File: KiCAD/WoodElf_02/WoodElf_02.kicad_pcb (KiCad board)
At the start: 2 copper layers, 19.2 x 19.2 mm, 14 parts

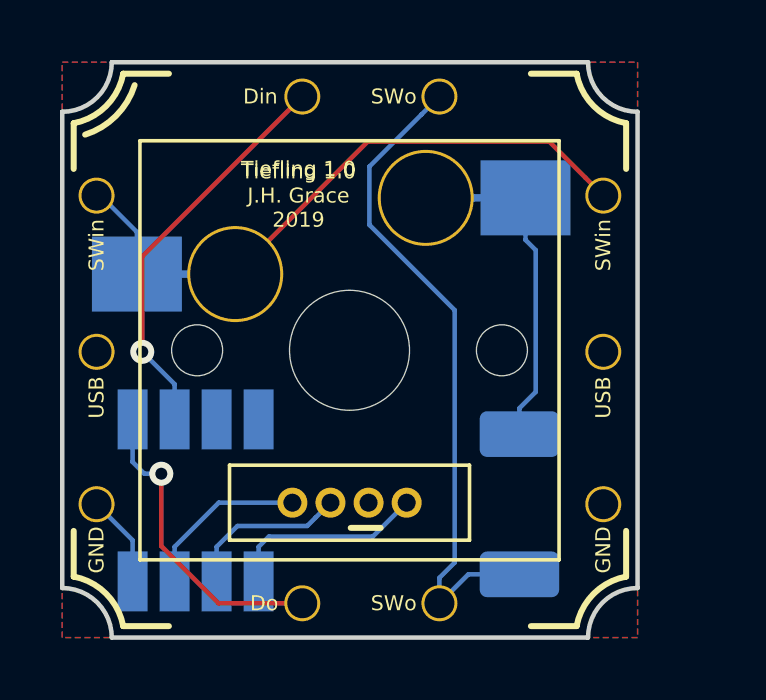
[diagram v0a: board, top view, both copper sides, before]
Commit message: updated the Tiefling PCB to better match real-world screw options
Also started mocking up the 3D-printed section
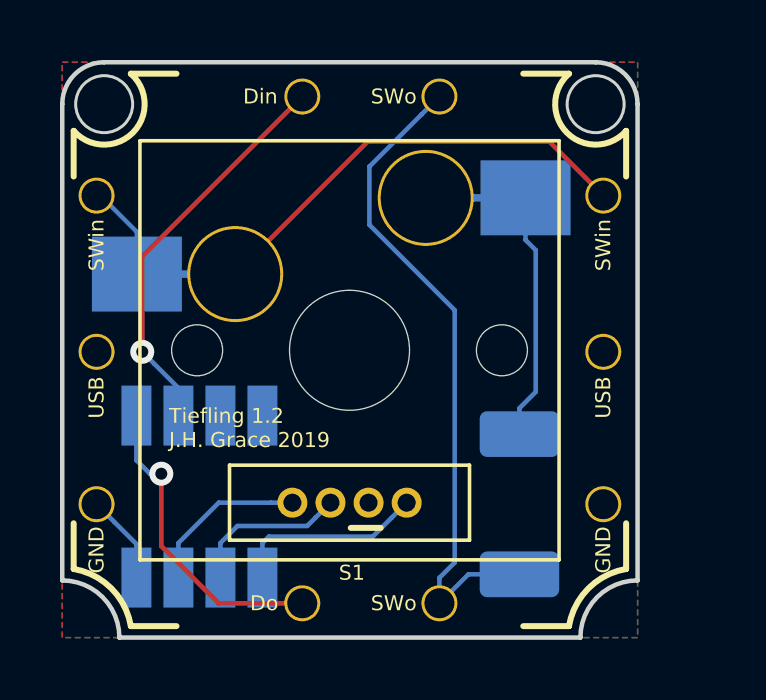
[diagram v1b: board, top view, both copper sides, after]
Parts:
- S1: renamed from Tiefling 1.0
- moved C 0.18 mm to (135.6, 112.5)
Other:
- outline, holes or cut-outs redrawn
- board text added: "Tiefling 1.2 J.H. Grace 2019"
- board text removed: "Tiefling 1.0 J.H. Grace 2019"

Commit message: completely redid the core code
it now uses a key matrix like any other sane keyboard does.  none of this slow-af I2C interface nonsense
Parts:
- added Mount: Mount, WoodElfLib:Mount, F.Cu at (132.5, 99.4)
- added Mount: Mount, WoodElfLib:Mount, F.Cu at (148.8, 99.4)
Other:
- outline, holes or cut-outs redrawn
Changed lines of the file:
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@@
   (general
     (thickness 1.6)
-    (drawings 36)
+    (drawings 34)
     (tracks 57)
     (zones 0)
-    (modules 14)
+    (modules 16)
     (nets 12)
   )
@@
     (add_net "Net-(D1-Pad1)")
   )
+  (module WoodElfLib:Mount (layer F.Cu)
+    (at 132.461 99.441)
+    (fp_text reference Mount (at 0 -1.397) (layer F.Fab)
+      (effects (font (size 0.5 0.5) (thickness 0.125)))
+    )
+    (fp_text value Mount (at 0 -1.397) (layer F.Fab)
+      (effects (font (size 0.5 0.5) (thickness 0.125)))
+    )
+    (pad "" np_thru_hole circle (at 0 0) (size 2 2) (drill 2) (layers *.Cu *.Mask))
+  )
+  (module WoodElfLib:Mount (layer F.Cu)
+    (at 148.844 99.441)
+    (fp_text reference Mount (at 0 -1.397) (layer F.Fab)
+      (effects (font (size 0.5 0.5) (thickness 0.125)))
+    )
+    (fp_text value Mount (at 0 -1.397) (layer F.Fab)
+      (effects (font (size 0.5 0.5) (thickness 0.125)))
+    )
+    (pad "" np_thru_hole circle (at 0 0) (size 2 2) (drill 2) (layers *.Cu *.Mask))
+  )
   (module WoodElfLib:SW_Cherry_MX1A_1.00u_PCB (layer F.Cu)
     (at 143.1798 102.5652)
@@
       (effects (font (size 1 1) (thickness 0.15)))
     )
+    (fp_line (start -10.414 12.954) (end -10.414 -2.794) (layer Dwgs.User) (width 0.15))
+    (fp_line (start 5.334 12.954) (end -10.414 12.954) (layer Dwgs.User) (width 0.15))
+    (fp_line (start 5.334 -2.794) (end 5.334 12.954) (layer Dwgs.User) (width 0.15))
+    (fp_line (start -10.393 -2.794) (end 5.334 -2.794) (layer Dwgs.User) (width 0.15))
+    (fp_line (start -9.525 12.065) (end -9.525 -1.905) (layer F.SilkS) (width 0.12))
+    (fp_line (start 4.445 12.065) (end -9.525 12.065) (layer F.SilkS) (width 0.12))
+    (fp_line (start 4.445 -1.905) (end 4.445 12.065) (layer F.SilkS) (width 0.12))
+    (fp_line (start -9.525 -1.905) (end 4.445 -1.905) (layer F.SilkS) (width 0.12))
+    (fp_line (start -12.065 14.605) (end -12.065 -4.445) (layer Dwgs.User) (width 0.15))
+    (fp_line (start 6.985 14.605) (end -12.065 14.605) (layer Dwgs.User) (width 0.15))
+    (fp_line (start 6.985 -4.445) (end 6.985 14.605) (layer Dwgs.User) (width 0.15))
+    (fp_line (start -12.065 -4.445) (end 6.985 -4.445) (layer Dwgs.User) (width 0.15))
+    (fp_line (start -9.14 -1.52) (end 4.06 -1.52) (layer F.CrtYd) (width 0.05))
+    (fp_line (start 4.06 -1.52) (end 4.06 11.68) (layer F.CrtYd) (width 0.05))
+    (fp_line (start 4.06 11.68) (end -9.14 11.68) (layer F.CrtYd) (width 0.05))
+    (fp_line (start -9.14 11.68) (end -9.14 -1.52) (layer F.CrtYd) (width 0.05))
+    (fp_text user %R (at -2.54 0) (layer F.Fab)
+      (effects (font (size 0.5 0.5) (thickness 0.125)))
+    )
+    (fp_line (start -6.54 8.91) (end -6.54 11.41) (layer F.SilkS) (width 0.12))
+    (fp_line (start -6.54 8.91) (end 1.46 8.91) (layer F.SilkS) (width 0.12))
+    (fp_line (start 1.46 8.91) (end 1.46 11.41) (layer F.SilkS) (width 0.12))
+    (fp_line (start -6.54 11.41) (end 1.46 11.41) (layer F.SilkS) (width 0.12))
     (fp_line (start -2.5 11) (end -1.5 11) (layer F.SilkS) (width 0.2))
-    (fp_line (start -6.54 11.41) (end 1.46 11.41) (layer F.SilkS) (width 0.12))
-    (fp_line (start 1.46 8.91) (end 1.46 11.41) (layer F.SilkS) (width 0.12))
-    (fp_line (start -6.54 8.91) (end 1.46 8.91) (layer F.SilkS) (width 0.12))
-    (fp_line (start -6.54 8.91) (end -6.54 11.41) (layer F.SilkS) (width 0.12))
-    (fp_text user %R (at -2.54 0) (layer F.Fab)
-      (effects (font (size 0.5 0.5) (thickness 0.125)))
-    )
-    (fp_line (start -9.14 11.68) (end -9.14 -1.52) (layer F.CrtYd) (width 0.05))
-    (fp_line (start 4.06 11.68) (end -9.14 11.68) (layer F.CrtYd) (width 0.05))
-    (fp_line (start 4.06 -1.52) (end 4.06 11.68) (layer F.CrtYd) (width 0.05))
-    (fp_line (start -9.14 -1.52) (end 4.06 -1.52) (layer F.CrtYd) (width 0.05))
-    (fp_line (start -12.065 -4.445) (end 6.985 -4.445) (layer Dwgs.User) (width 0.15))
-    (fp_line (start 6.985 -4.445) (end 6.985 14.605) (layer Dwgs.User) (width 0.15))
-    (fp_line (start 6.985 14.605) (end -12.065 14.605) (layer Dwgs.User) (width 0.15))
-    (fp_line (start -12.065 14.605) (end -12.065 -4.445) (layer Dwgs.User) (width 0.15))
-    (fp_line (start -9.525 -1.905) (end 4.445 -1.905) (layer F.SilkS) (width 0.12))
-    (fp_line (start 4.445 -1.905) (end 4.445 12.065) (layer F.SilkS) (width 0.12))
-    (fp_line (start 4.445 12.065) (end -9.525 12.065) (layer F.SilkS) (width 0.12))
-    (fp_line (start -9.525 12.065) (end -9.525 -1.905) (layer F.SilkS) (width 0.12))
+    (pad "" np_thru_hole circle (at 2.54 5.08) (size 1.7 1.7) (drill 1.7) (layers *.Cu *.Mask))
+    (pad "" np_thru_hole circle (at -7.62 5.08) (size 1.7 1.7) (drill 1.7) (layers *.Cu *.Mask))
+    (pad "" np_thru_hole circle (at -2.54 5.08) (size 4 4) (drill 4) (layers *.Cu *.Mask))
+    (pad 2 thru_hole circle (at -6.35 2.54) (size 3.2 3.2) (drill 3) (layers *.Cu *.Mask)
+      (net 11 /SWIN))
+    (pad 1 thru_hole circle (at 0 0) (size 3.2 3.2) (drill 3) (layers *.Cu *.Mask)
+      (net 6 "Net-(D1-Pad1)"))
+    (pad 5 thru_hole circle (at -3.175 10.16) (size 1 1) (drill 0.6) (layers *.Cu *.Mask)
+      (net 1 "Net-(C1-Pad2)") (solder_mask_margin 0.1) (clearance 0.01))
+    (pad 6 thru_hole circle (at -4.445 10.16) (size 1 1) (drill 0.6) (layers *.Cu *.Mask)
+      (net 2 "Net-(C1-Pad3)") (solder_mask_margin 0.1) (clearance 0.01))
+    (pad 4 thru_hole circle (at -1.905 10.16 45) (size 1 1) (drill 0.6) (layers *.Cu *.Mask)
+      (net 5 /USB) (solder_mask_margin 0.1) (clearance 0.01))
     (pad 3 thru_hole circle (at -0.635 10.16) (size 1 1) (drill 0.6) (layers *.Cu *.Mask)
       (net 3 "Net-(C1-Pad1)") (solder_mask_margin 0.1) (clearance 0.01))
-    (pad 4 thru_hole circle (at -1.905 10.16 45) (size 1 1) (drill 0.6) (layers *.Cu *.Mask)
-      (net 5 /USB) (solder_mask_margin 0.1) (clearance 0.01))
-    (pad 6 thru_hole circle (at -4.445 10.16) (size 1 1) (drill 0.6) (layers *.Cu *.Mask)
-      (net 2 "Net-(C1-Pad3)") (solder_mask_margin 0.1) (clearance 0.01))
-    (pad 5 thru_hole circle (at -3.175 10.16) (size 1 1) (drill 0.6) (layers *.Cu *.Mask)
-      (net 1 "Net-(C1-Pad2)") (solder_mask_margin 0.1) (clearance 0.01))
-    (pad 1 thru_hole circle (at 0 0) (size 3.2 3.2) (drill 3) (layers *.Cu *.Mask)
-      (net 6 "Net-(D1-Pad1)"))
-    (pad 2 thru_hole circle (at -6.35 2.54) (size 3.2 3.2) (drill 3) (layers *.Cu *.Mask)
-      (net 11 /SWIN))
-    (pad "" np_thru_hole circle (at -2.54 5.08) (size 4 4) (drill 4) (layers *.Cu *.Mask))
-    (pad "" np_thru_hole circle (at -7.62 5.08) (size 1.7 1.7) (drill 1.7) (layers *.Cu *.Mask))
-    (pad "" np_thru_hole circle (at 2.54 5.08) (size 1.7 1.7) (drill 1.7) (layers *.Cu *.Mask))
     (model ${KISYS3DMOD}/Button_Switch_Keyboard.3dshapes/SW_Cherry_MX1A_1.00u_PCB.wrl
       (at (xyz 0 0 0))
@@
   )
   (gr_arc (start 148.844 99.441) (end 147.955 98.425) (angle -187.6281497) (layer B.SilkS) (width 0.2))
-  (gr_circle (center 132.461 99.441) (end 133.411 99.441) (layer Edge.Cuts) (width 0.1))
-  (gr_circle (center 148.844 99.441) (end 149.794 99.441) (layer Edge.Cuts) (width 0.1))
   (gr_line (start 147.955 98.425) (end 146.431 98.425) (layer B.SilkS) (width 0.2))
   (gr_line (start 149.86 100.33) (end 149.86 101.854) (layer B.SilkS) (width 0.2))

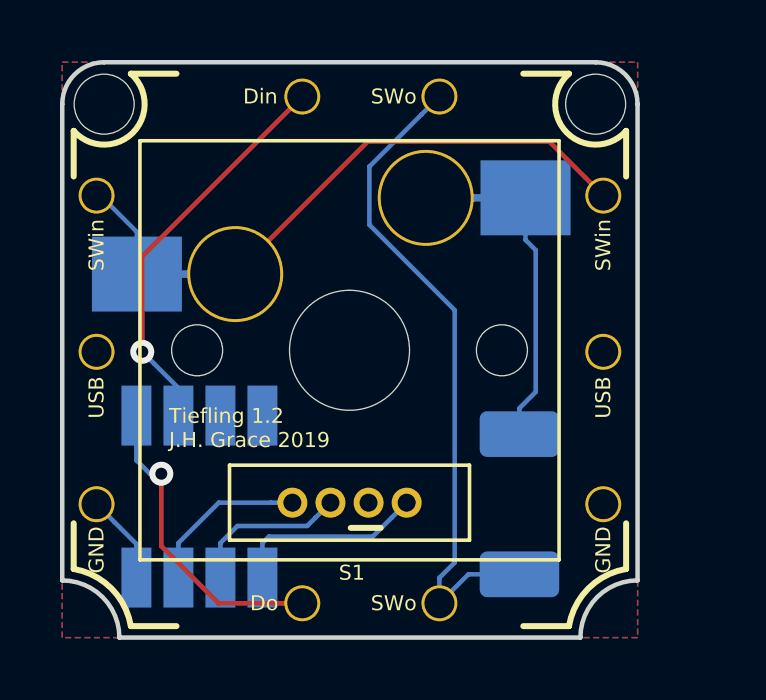
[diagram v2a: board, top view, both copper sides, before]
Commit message: updated PCB to support screws in all corners
rotated the MS2811 chip to allow for all four corners to be screwed in for support.  still need to adjust the holes around the edges though
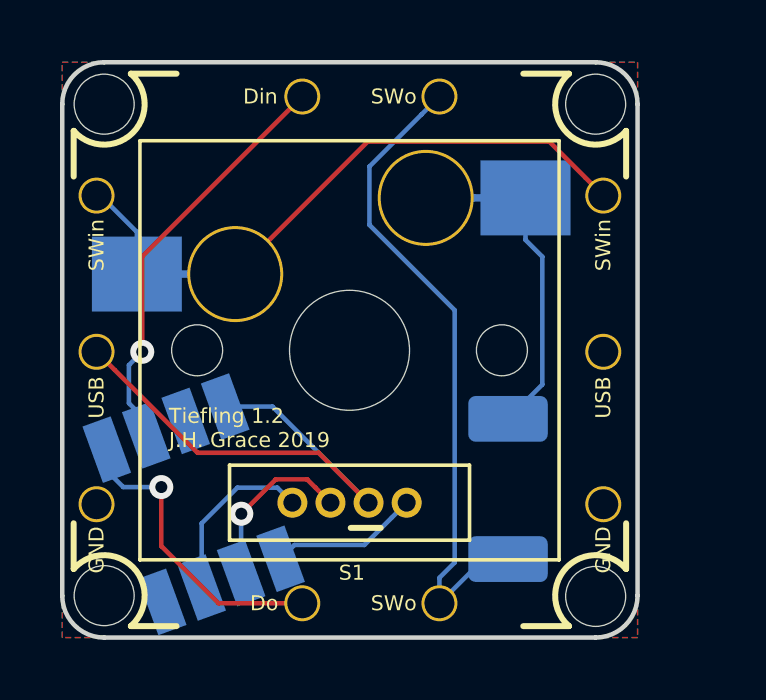
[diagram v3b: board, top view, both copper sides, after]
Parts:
- added Mount: Mount, WoodElfLib:Mount, F.Cu at (132.5, 115.8)
- added Mount: Mount, WoodElfLib:Mount, F.Cu at (148.8, 115.8)
- moved D 0.63 mm to (145.9, 112.3)
- moved C 0.32 mm to (135.4, 112.8), turned to 200 degrees
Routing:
- net /USB: track 0.00 -> 17.3 mm
- net /GND: track 3.00 -> 0.00 mm
- net Net-(C1-Pad1): track 6.52 -> 4.98 mm
- net Net-(D1-Pad1): track 11.5 -> 12.2 mm
- net /DIN: track 14.1 -> 14.7 mm
- net Net-(C1-Pad2): track 5.38 -> 5.75 mm, vias 0 -> 1
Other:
- outline, holes or cut-outs redrawn

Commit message: updated the PCB to use a 2x2mm SMD RGB LED
hopefully this works.  i want to avoid relying solely on adafruit for their 5x2mm square RGB LED, and i needed more space to allow for the screw mounts.
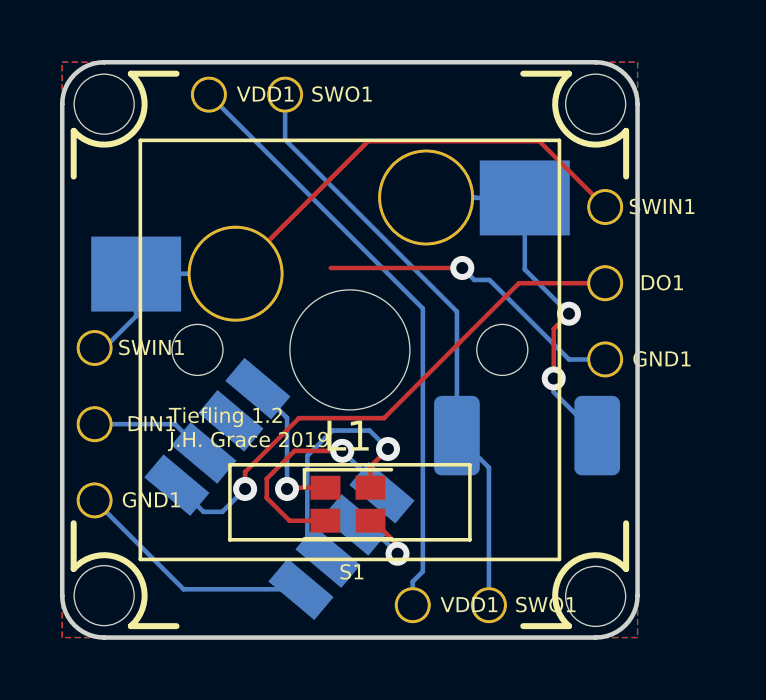
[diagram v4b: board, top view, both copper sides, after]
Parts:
- removed C: WS2811, WoodElfLib:WS2811
- removed D: DIODE, WoodElfLib:D_2010_5025Metric_Pad1.52x2.65mm_HandSolder
- removed Din, Do, GND (x2), SWin (x2), SWo (x2), USB (x2): BTH, WoodElfLib:BlankThrough-Hole
- removed H: Kailh_HotSwap_SwitchMount, WoodElfLib:Kailh_HotSwap_Socket
- added C1: WS2811, WoodElf_Lib:WS2811, B.Cu at (138.3, 112.3)
- added D1: DIODE, Diode_SMD:D_2010_5025Metric_Pad1.52x2.65mm_HandSolder, B.Cu at (146.6, 110.5)
- added DIN1: BlankThrough-Hole, WoodElf_Lib:BlankThrough-Hole, F.Cu at (132.1, 110.1)
- added DO1: BlankThrough-Hole, WoodElf_Lib:BlankThrough-Hole, F.Cu at (149.2, 105.4)
- added GND1: BlankThrough-Hole, WoodElf_Lib:BlankThrough-Hole, F.Cu at (149.2, 108.0)
- added GND1: BlankThrough-Hole, WoodElf_Lib:BlankThrough-Hole, F.Cu at (132.1, 112.6)
- added H1: Kailh_HotSwap_SwitchMount, WoodElf_Lib:Kailh_HotSwap_Socket, F.Cu at (143.2, 102.6)
- added L1: LED_ARGB, LED_SMD:LED_Cree-PLCC4_2x2mm_CW, F.Cu at (140.6, 112.8)
- added SWIN1: BlankThrough-Hole, WoodElf_Lib:BlankThrough-Hole, F.Cu at (149.2, 102.9)
- added SWIN1: BlankThrough-Hole, WoodElf_Lib:BlankThrough-Hole, F.Cu at (132.1, 107.6)
- added SWO1: BlankThrough-Hole, WoodElf_Lib:BlankThrough-Hole, F.Cu at (145.3, 116.1)
- added SWO1: BlankThrough-Hole, WoodElf_Lib:BlankThrough-Hole, F.Cu at (138.5, 99.1)
- added VDD1: BlankThrough-Hole, WoodElf_Lib:BlankThrough-Hole, F.Cu at (142.7, 116.1)
- added VDD1: BlankThrough-Hole, WoodElf_Lib:BlankThrough-Hole, F.Cu at (136.0, 99.1)
- S1: footprint WoodElfLib:SW_Cherry_MX1A_1.00u_PCB -> WoodElf_Lib:SW_Cherry_MX1A_1.00u_PCB
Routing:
- net /GND: track 0.00 -> 18.5 mm, vias 0 -> 1
- net /DIN: track 14.7 -> 4.04 mm, vias 1 -> 0
- net /USB: track 17.3 -> 25.5 mm, vias 0 -> 1
- net /DO: track 10.2 -> 18.1 mm
- net Net-(C1-Pad1): track 4.98 -> 7.76 mm, vias 0 -> 1
- net Net-(C1-Pad3): track 5.86 -> 8.49 mm, vias 0 -> 1
- net Net-(C1-Pad2): track 5.75 -> 3.35 mm
- net /SWO: track 22.1 -> 19.8 mm
- net /SWIN: track 21.4 -> 22.0 mm
- net Net-(D1-Pad1): track 12.2 -> 12.6 mm, vias 0 -> 2

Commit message: re-wrote how the pressed keys are stored to avoid going over the 6-key limit
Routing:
- net /GND: track 18.5 -> 30.7 mm
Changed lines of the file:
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@@
     (thickness 1.6)
     (drawings 38)
-    (tracks 76)
+    (tracks 80)
     (zones 0)
     (modules 19)
@@
     (34 B.Paste user hide)
     (35 F.Paste user hide)
-    (36 B.SilkS user)
+    (36 B.SilkS user hide)
     (37 F.SilkS user)
-    (38 B.Mask user)
+    (38 B.Mask user hide)
     (39 F.Mask user)
     (40 Dwgs.User user)
-    (41 Cmts.User user)
+    (41 Cmts.User user hide)
     (42 Eco1.User user hide)
     (43 Eco2.User user hide)
     (44 Edge.Cuts user)
-    (45 Margin user)
-    (46 B.CrtYd user)
+    (45 Margin user hide)
+    (46 B.CrtYd user hide)
     (47 F.CrtYd user)
-    (48 B.Fab user)
-    (49 F.Fab user)
+    (48 B.Fab user hide)
+    (49 F.Fab user hide)
   )
   (setup
@@
   (segment (start 147.955 106.426) (end 146.4818 104.9528) (width 0.1524) (layer B.Cu) (net 6))
   (via (at 144.399 104.902) (size 0.8) (drill 0.4) (layers F.Cu B.Cu) (net 7))
-  (segment (start 140.014222 104.902) (end 144.399 104.902) (width 0.1524) (layer F.Cu) (net 7))
   (segment (start 135.10672 115.61222) (end 132.1435 112.649) (width 0.1524) (layer B.Cu) (net 7))
   (segment (start 139.021466 115.61222) (end 135.10672 115.61222) (width 0.1524) (layer B.Cu) (net 7))
@@
   (segment (start 149.1615 107.95) (end 147.955 107.95) (width 0.1524) (layer B.Cu) (net 7))
   (segment (start 147.955 107.95) (end 145.306999 105.301999) (width 0.1524) (layer B.Cu) (net 7))
+  (segment (start 134.0485 112.649) (end 132.1435 112.649) (width 0.1524) (layer F.Cu) (net 7))
+  (segment (start 137.414 109.2835) (end 134.0485 112.649) (width 0.1524) (layer F.Cu) (net 7))
+  (segment (start 137.414 107.457778) (end 137.414 109.2835) (width 0.1524) (layer F.Cu) (net 7))
+  (segment (start 144.399 104.902) (end 139.969778 104.902) (width 0.1524) (layer F.Cu) (net 7))
+  (segment (start 139.969778 104.902) (end 137.414 107.457778) (width 0.1524) (layer F.Cu) (net 7))
   (segment (start 135.784729 111.068705) (end 134.825024 110.109) (width 0.1524) (layer B.Cu) (net 8))
   (segment (start 134.825024 110.109) (end 132.1435 110.109) (width 0.1524) (layer B.Cu) (net 8))
